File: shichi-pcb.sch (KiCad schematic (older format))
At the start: 22 parts, among them J1 USB_C_Receptacle_HRO_TYPE-C-3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, J2 Conn_01x04_Male, J3 Conn_01x06_Male, SW1 SW_Push, U1 USBLC6-2SC6, U2 ATmega32U4-AU, Y1 Crystal_GND24

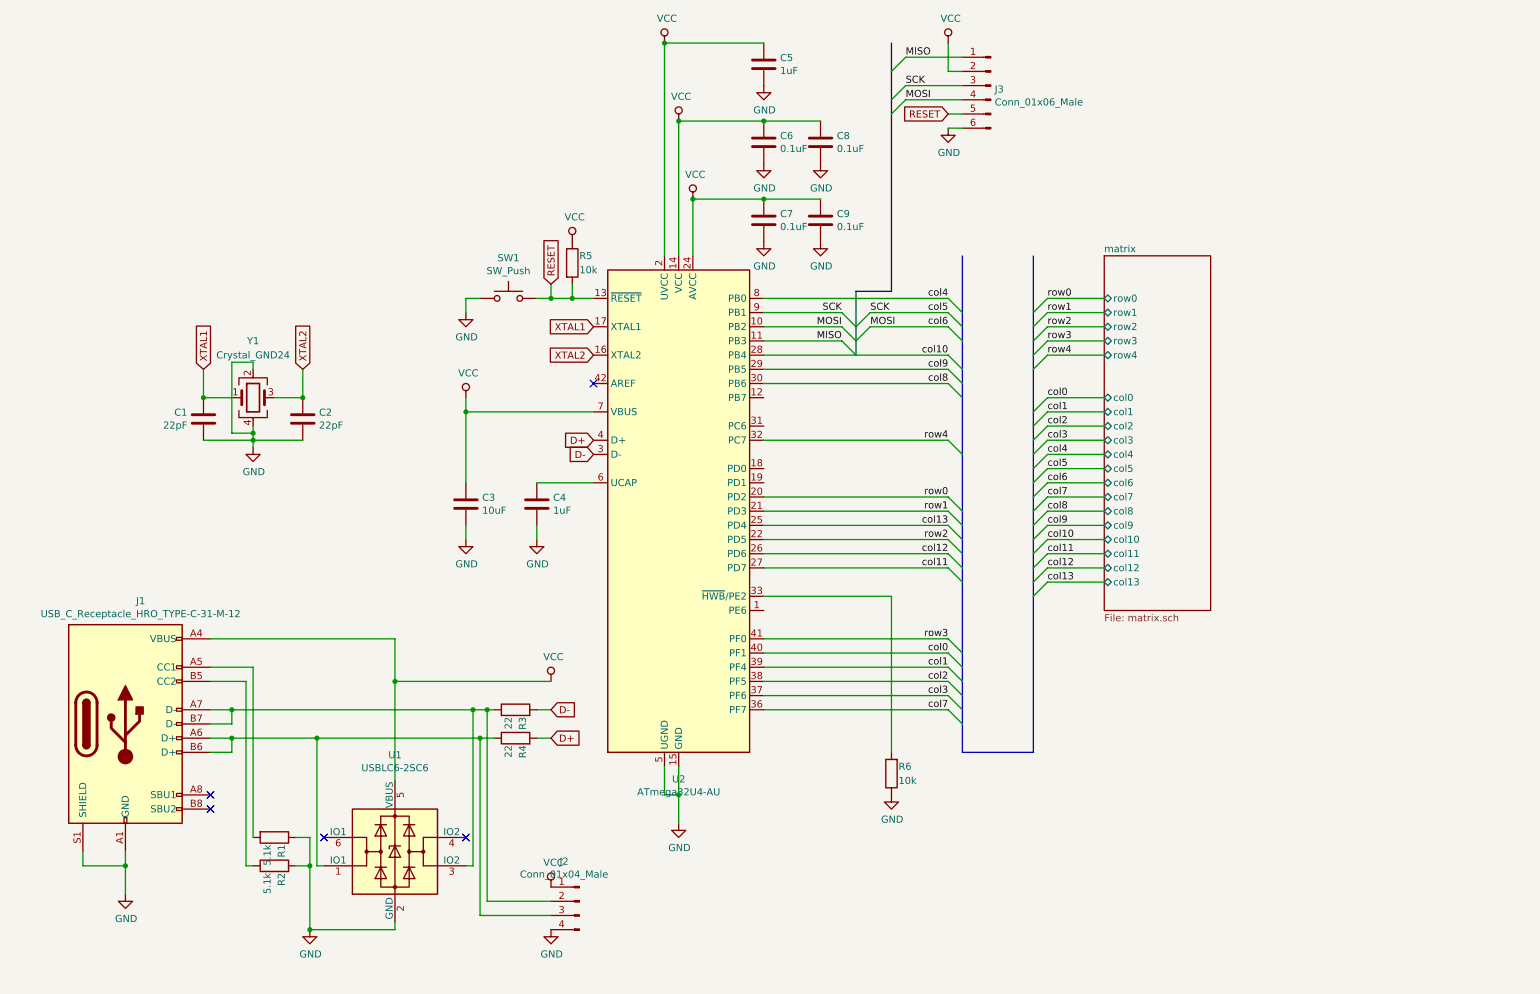
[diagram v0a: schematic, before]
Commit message: Add breakouts for unused pins
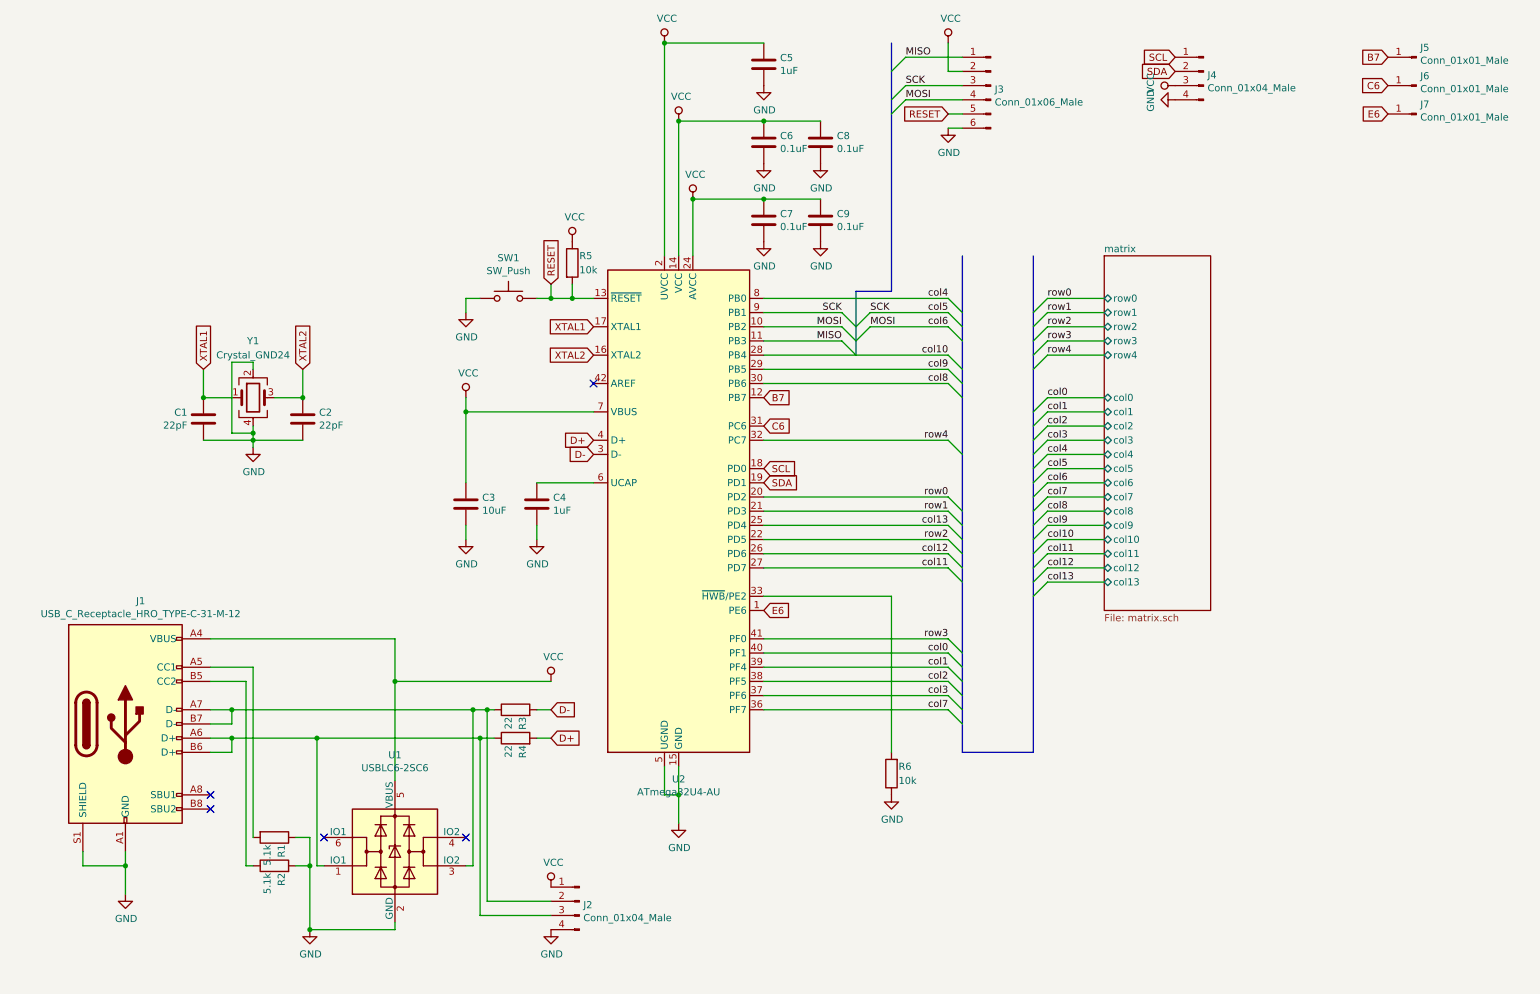
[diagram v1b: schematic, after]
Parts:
- added J4: Conn_01x04_Male, Connector_PinHeader_2.54mm:PinHeader_1x04_P2.54mm_Vertical, symbol Connector:Conn_01x04_Male
- added J5, J6, J7: Conn_01x01_Male, Connector_PinHeader_2.54mm:PinHeader_1x01_P2.54mm_Vertical, symbol Connector:Conn_01x01_Male
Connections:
- net GND: now also J4.4 (Pin_4)
- net VCC: now also J4.3 (Pin_3)
- net E6: now reaches U2.1 (PE6)
- net E6: now also J7.1 (Pin_1)
- net B7: now reaches U2.12 (PB7)
- net B7: now also J5.1 (Pin_1)
- net SCL: now reaches U2.18 (PD0)
- net SCL: now also J4.1 (Pin_1)
- net SDA: now reaches U2.19 (PD1)
- net SDA: now also J4.2 (Pin_2)
- net C6: now reaches U2.31 (PC6)
- net C6: now also J6.1 (Pin_1)
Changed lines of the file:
@@
 	4100 2800 4250 2800
 Connection ~ 4100 2800
-Wire Wire Line
-	6600 1100 7000 1100
 Entry Wire Line
 	6600 1100 6500 1200
@@
 Wire Wire Line
 	7000 1200 6900 1200
-Wire Wire Line
-	6900 1200 6900 1000
 Wire Wire Line
 	5000 6500 5000 6300
@@
 $EndComp
 $Comp
-L Connector:Conn_01x04_Male J2
-U 1 1 5D041F2E
-P 4300 7050
-F 0 "J2" H 4408 7331 50  0000 C CNN
-F 1 "Conn_01x04_Male" H 4408 7240 50  0000 C CNN
-F 2 "Connector_PinHeader_2.54mm:PinHeader_1x04_P2.54mm_Vertical" H 4300 7050 50  0001 C CNN
-F 3 "~" H 4300 7050 50  0001 C CNN
-	1    4300 7050
-	-1   0    0    -1
-$EndComp
-$Comp
 L power:GND #PWR010
 U 1 1 5CFB0CA6
@@
 	1    0    0    -1
 $EndComp
+Text GLabel 6900 1500 0    50   Input ~ 0
+RESET
+Wire Wire Line
+	4000 5900 4100 5900
+$Comp
+L Device:R R4
+U 1 1 5CFC0556
+P 3850 5900
+F 0 "R4" H 3800 5850 50  0000 R CNN
+F 1 "22" H 3800 5950 50  0000 R CNN
+F 2 "Resistor_SMD:R_0805_2012Metric_Pad1.15x1.40mm_HandSolder" V 3780 5900 50  0001 C CNN
+F 3 "~" H 3850 5900 50  0001 C CNN
+	1    3850 5900
+	0    -1   -1   0
+$EndComp
+Wire Wire Line
+	3650 5700 3650 7050
+Wire Wire Line
+	3650 7050 4100 7050
+Connection ~ 3650 5700
+Wire Wire Line
+	3650 5700 3700 5700
+Wire Wire Line
+	3550 5700 3650 5700
+Wire Wire Line
+	3600 5900 3600 7150
+Wire Wire Line
+	3600 7150 4100 7150
+Connection ~ 3600 5900
+Wire Wire Line
+	3600 5900 3700 5900
+Wire Wire Line
+	2000 3850 2000 3800
+Wire Wire Line
+	2350 3800 2000 3800
+Connection ~ 2000 3800
+Wire Wire Line
+	1650 3800 2000 3800
+Wire Wire Line
+	2000 3700 2000 3750
+Connection ~ 2000 3750
+Wire Wire Line
+	2000 3750 2000 3800
+Text GLabel 5600 4100 2    50   Input ~ 0
+SDA
+Text GLabel 5600 4000 2    50   Input ~ 0
+SCL
+Text GLabel 8500 1100 0    50   Input ~ 0
+SCL
+Text GLabel 8500 1200 0    50   Input ~ 0
+SDA
+Wire Wire Line
+	6900 1200 6900 1000
+Wire Wire Line
+	6600 1100 7000 1100
 $Comp
 L Connector:Conn_01x06_Male J3
@@
 	-1   0    0    -1
 $EndComp
-Text GLabel 6900 1500 0    50   Input ~ 0
-RESET
-Wire Wire Line
-	4000 5900 4100 5900
-$Comp
-L Device:R R4
-U 1 1 5CFC0556
-P 3850 5900
-F 0 "R4" H 3800 5850 50  0000 R CNN
-F 1 "22" H 3800 5950 50  0000 R CNN
-F 2 "Resistor_SMD:R_0805_2012Metric_Pad1.15x1.40mm_HandSolder" V 3780 5900 50  0001 C CNN
-F 3 "~" H 3850 5900 50  0001 C CNN
-	1    3850 5900
+$Comp
+L power:VCC #PWR024
+U 1 1 5D01C4D7
+P 8500 1300
+F 0 "#PWR024" H 8500 1150 50  0001 C CNN
+F 1 "VCC" H 8517 1473 50  0000 C CNN
+F 2 "" H 8500 1300 50  0001 C CNN
+F 3 "" H 8500 1300 50  0001 C CNN
+	1    8500 1300
 	0    -1   -1   0
 $EndComp
-Wire Wire Line
-	3650 5700 3650 7050
-Wire Wire Line
-	3650 7050 4100 7050
-Connection ~ 3650 5700
-Wire Wire Line
-	3650 5700 3700 5700
-Wire Wire Line
-	3550 5700 3650 5700
-Wire Wire Line
-	3600 5900 3600 7150
-Wire Wire Line
-	3600 7150 4100 7150
-Connection ~ 3600 5900
-Wire Wire Line
-	3600 5900 3700 5900
-Wire Wire Line
-	2000 3850 2000 3800
-Wire Wire Line
-	2350 3800 2000 3800
-Connection ~ 2000 3800
-Wire Wire Line
-	1650 3800 2000 3800
-Wire Wire Line
-	2000 3700 2000 3750
-Connection ~ 2000 3750
-Wire Wire Line
-	2000 3750 2000 3800
+$Comp
+L power:GND #PWR025
+U 1 1 5D01D767
+P 8500 1400
+F 0 "#PWR025" H 8500 1150 50  0001 C CNN
+F 1 "GND" H 8505 1227 50  0000 C CNN
+F 2 "" H 8500 1400 50  0001 C CNN
+F 3 "" H 8500 1400 50  0001 C CNN
+	1    8500 1400
+	0    1    1    0
+$EndComp
+Text GLabel 5600 3500 2    50   Input ~ 0
+B7
+Text GLabel 5600 3700 2    50   Input ~ 0
+C6
+Text GLabel 5600 5000 2    50   Input ~ 0
+E6
+$Comp
+L Connector:Conn_01x01_Male J5
+U 1 1 5D07EA53
+P 10200 1100
+F 0 "J5" H 10172 1032 50  0000 R CNN
+F 1 "Conn_01x01_Male" H 10172 1123 50  0000 R CNN
+F 2 "Connector_PinHeader_2.54mm:PinHeader_1x01_P2.54mm_Vertical" H 10200 1100 50  0001 C CNN
+F 3 "~" H 10200 1100 50  0001 C CNN
+	1    10200 1100
+	-1   0    0    1
+$EndComp
+$Comp
+L Connector:Conn_01x01_Male J6
+U 1 1 5D07FB62
+P 10200 1300
+F 0 "J6" H 10172 1232 50  0000 R CNN
+F 1 "Conn_01x01_Male" H 10172 1323 50  0000 R CNN
+F 2 "Connector_PinHeader_2.54mm:PinHeader_1x01_P2.54mm_Vertical" H 10200 1300 50  0001 C CNN
+F 3 "~" H 10200 1300 50  0001 C CNN
+	1    10200 1300
+	-1   0    0    1
+$EndComp
+$Comp
+L Connector:Conn_01x01_Male J7
+U 1 1 5D080441
+P 10200 1500
+F 0 "J7" H 10172 1432 50  0000 R CNN
+F 1 "Conn_01x01_Male" H 10172 1523 50  0000 R CNN
+F 2 "Connector_PinHeader_2.54mm:PinHeader_1x01_P2.54mm_Vertical" H 10200 1500 50  0001 C CNN
+F 3 "~" H 10200 1500 50  0001 C CNN
+	1    10200 1500
+	-1   0    0    1
+$EndComp
+Text GLabel 10000 1100 0    50   Input ~ 0
+B7
+Text GLabel 10000 1300 0    50   Input ~ 0
+C6
+Text GLabel 10000 1500 0    50   Input ~ 0
+E6
+$Comp
+L Connector:Conn_01x04_Male J2
+U 1 1 5D000828
+P 4300 7050
+F 0 "J2" H 4272 7024 50  0000 R CNN
+F 1 "Conn_01x04_Male" H 4272 6933 50  0000 R CNN
+F 2 "Connector_PinHeader_2.54mm:PinHeader_1x04_P2.54mm_Vertical" H 4300 7050 50  0001 C CNN
+F 3 "~" H 4300 7050 50  0001 C CNN
+	1    4300 7050
+	-1   0    0    -1
+$EndComp
+$Comp
+L Connector:Conn_01x04_Male J4
+U 1 1 5D005F7A
+P 8700 1200
+F 0 "J4" H 8672 1174 50  0000 R CNN
+F 1 "Conn_01x04_Male" H 8672 1083 50  0000 R CNN
+F 2 "Connector_PinHeader_2.54mm:PinHeader_1x04_P2.54mm_Vertical" H 8700 1200 50  0001 C CNN
+F 3 "~" H 8700 1200 50  0001 C CNN
+	1    8700 1200
+	-1   0    0    -1
+$EndComp
 Wire Wire Line
 	5600 3200 6900 3200
